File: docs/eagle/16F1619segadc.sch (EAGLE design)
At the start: 21 parts, among them IC1 74HC595N, IC2 PIC16F1619, T1 2N2222, T2 2N2222, T3 2N2222, T4 2N2222

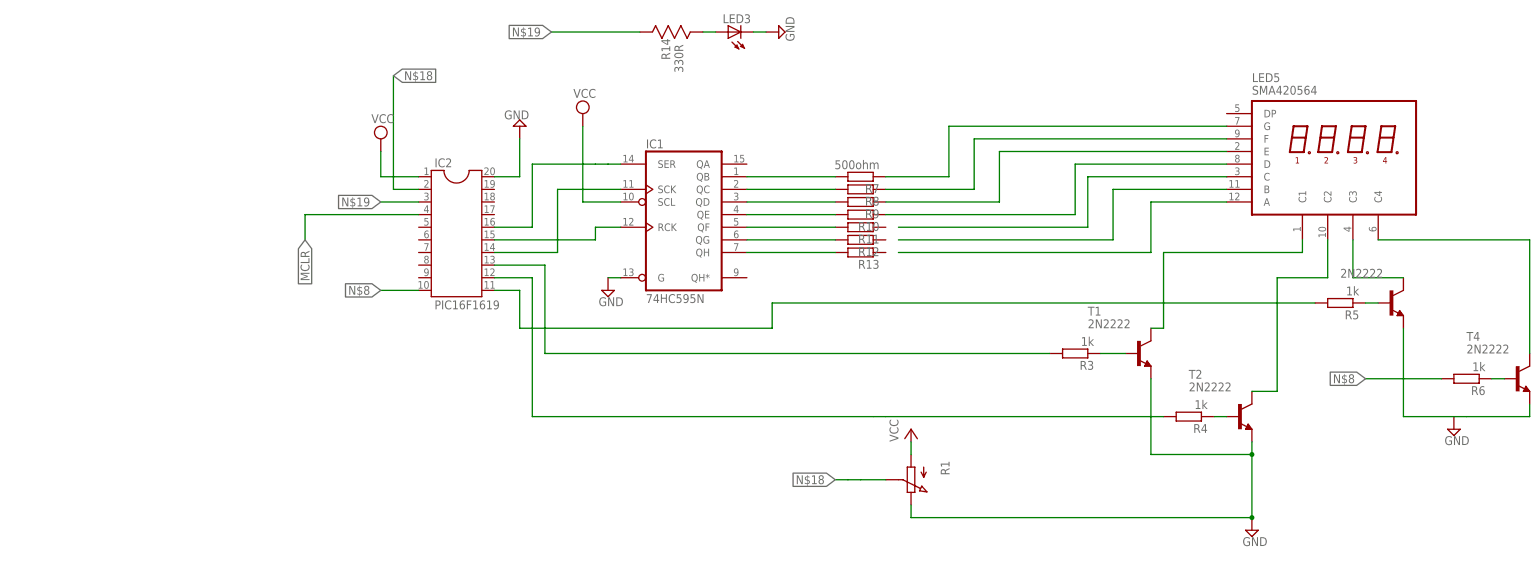
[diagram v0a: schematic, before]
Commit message: change eagle footprint for pic16f1619
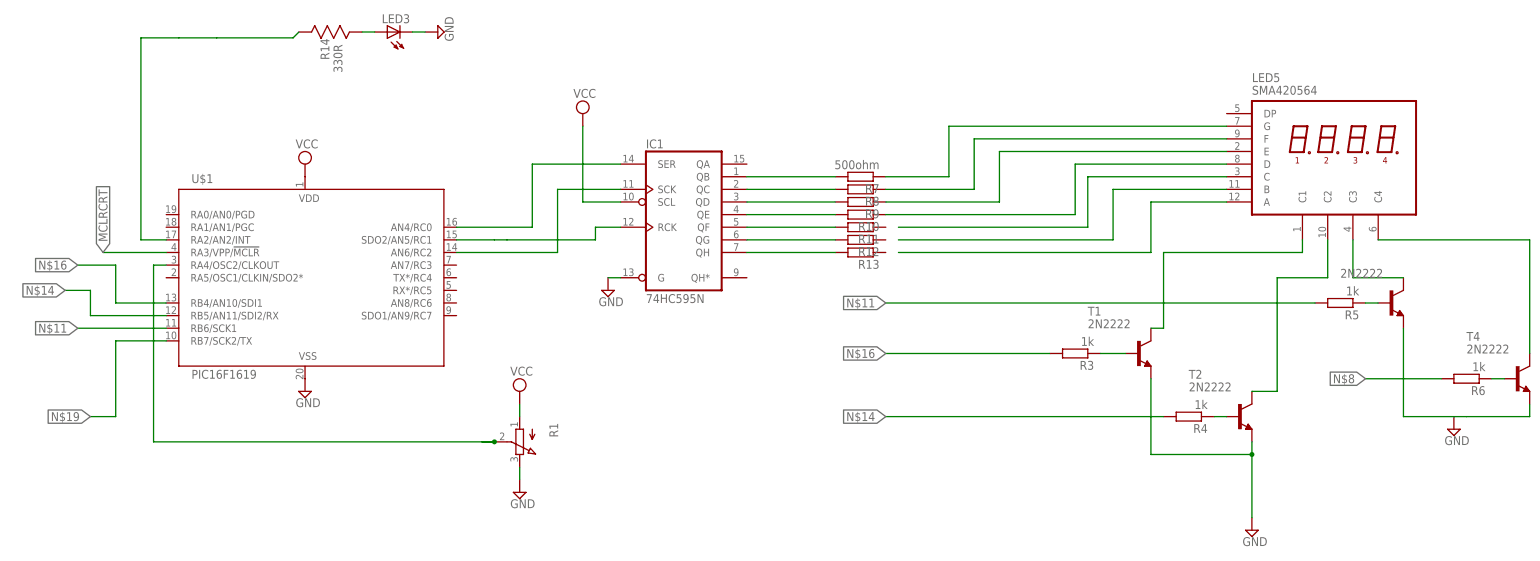
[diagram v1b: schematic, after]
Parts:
- removed IC2: PIC16F1619, ic-package:DIL20
- added U$1: PIC16F1619, SparkFun-IC-Microcontroller:PIC16F1829
- R1: device pot-vitrohm:PC25 -> pot:3RP/1610N
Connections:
- removed net MCLR: IC2.4
- new net MCLRCRT: U$1.RA3/VPP/!MCLR
- net GND: now also U$1.VSS; no longer IC2.20
- net N$1: now also R1.S, U$1.RA4/OSC2/CLKOUT; no longer IC2.10
- net N$11: now also U$1.RB6/SCK1; no longer IC2.11
- net N$14: now also U$1.RB5/AN11/SDI2/RX; no longer IC2.12
- net N$16: now also U$1.RB4/AN10/SDI1; no longer IC2.13
- net N$18: now also R14.R1, U$1.RA2/AN2/INT; no longer IC2.2, R1.S
- net N$19: now also U$1.RB7/SCK2/TX; no longer IC2.3, R14.R1
- net N$3: now also U$1.AN6/RC2; no longer IC2.14
- net N$4: now also U$1.SDO2/AN5/RC1; no longer IC2.15
- net N$7: now also U$1.AN4/RC0; no longer IC2.16
- net VCC: now also U$1.VDD; no longer IC2.1
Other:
- moved on the sheet: LED3, R14

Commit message: adding  new  eagle library footprint to schematic for SMA420564
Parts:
- removed LED5: SMA420564, hp-displays:5082-7414
- added SMA420564: NFD-5641AS, display-nfd:NFD-5641AS
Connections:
- removed net N$8: R6.2
- net N$10: now also SMA420564.P$5; no longer LED5.G
- net N$19: now also R6.2
- net N$2: now also SMA420564.P$9; no longer LED5.C2
- net N$24: now also SMA420564.P$8; no longer LED5.C3
- net N$25: now also SMA420564.P$6; no longer LED5.C4
- net N$26: now also SMA420564.P$11; no longer LED5.A
- net N$27: now also SMA420564.P$7; no longer LED5.B
- net N$28: now also SMA420564.P$1; no longer LED5.E
- net N$29: now also SMA420564.P$4; no longer LED5.C
- net N$30: now also SMA420564.P$2; no longer LED5.D
- net N$5: now also SMA420564.P$12; no longer LED5.C1
- net N$9: now also SMA420564.P$10; no longer LED5.F
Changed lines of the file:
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@@
 <?xml version="1.0" encoding="utf-8"?>
 <!DOCTYPE eagle SYSTEM "eagle.dtd">
-<eagle version="9.3.0">
+<eagle version="9.3.1">
 <drawing>
 <settings>
@@
 <part name="R12" library="eagle-ltspice" library_urn="urn:adsk.eagle:library:217" deviceset="R" device="0204/7" package3d_urn="urn:adsk.eagle:package:13274/1"/>
 <part name="R13" library="eagle-ltspice" library_urn="urn:adsk.eagle:library:217" deviceset="R" device="0204/7" package3d_urn="urn:adsk.eagle:package:13274/1"/>
-<part name="LED5" library="hp-displays" deviceset="5082-7414" device="" value="SMA420564"/>
 <part name="IC1" library="74xx-eu" library_urn="urn:adsk.eagle:library:85" deviceset="74*595" device="N" package3d_urn="urn:adsk.eagle:package:922/2" technology="HC"/>
 <part name="SUPPLY2" library="supply2" library_urn="urn:adsk.eagle:library:372" deviceset="GND" device=""/>
@@
 <part name="SUPPLY7" library="supply2" library_urn="urn:adsk.eagle:library:372" deviceset="GND" device=""/>
 <part name="SUPPLY8" library="supply2" library_urn="urn:adsk.eagle:library:372" deviceset="VCC" device=""/>
+<part name="SMA420564" library="display-nfd" deviceset="NFD-5641AS" device=""/>
 </parts>
 <sheets>
@@
 <attribute name="VALUE" x="85.09" y="64.262" size="1.778" layer="96" rot="R180"/>
 </instance>
-<instance part="LED5" gate="$1" x="160.02" y="91.44" smashed="yes">
-<attribute name="NAME" x="160.02" y="95.25" size="1.778" layer="95"/>
-<attribute name="VALUE" x="160.02" y="92.71" size="1.778" layer="96"/>
-</instance>
 <instance part="IC1" gate="A" x="45.72" y="68.58" smashed="yes">
 <attribute name="NAME" x="38.1" y="81.915" size="1.778" layer="95"/>
@@
 <instance part="SUPPLY8" gate="G$1" x="12.7" y="33.02" smashed="yes">
 <attribute name="VALUE" x="10.795" y="36.195" size="1.778" layer="96"/>
+</instance>
+<instance part="SMA420564" gate="G$1" x="165.1" y="78.74" smashed="yes" rot="MR270">
+<attribute name="NAME" x="170.18" y="94.107" size="1.778" layer="95" rot="MR0"/>
 </instance>
 </instances>
@@
 <wire x1="165.1" y1="33.02" x2="160.02" y2="33.02" width="0.1524" layer="91"/>
 <wire x1="165.1" y1="55.88" x2="165.1" y2="33.02" width="0.1524" layer="91"/>
-<pinref part="LED5" gate="$1" pin="C2"/>
-<wire x1="175.26" y1="63.5" x2="175.26" y2="55.88" width="0.1524" layer="91"/>
-<wire x1="175.26" y1="55.88" x2="165.1" y2="55.88" width="0.1524" layer="91"/>
+<wire x1="165.1" y1="55.88" x2="175.26" y2="55.88" width="0.1524" layer="91"/>
+<wire x1="175.26" y1="55.88" x2="175.26" y2="63.5" width="0.1524" layer="91"/>
+<wire x1="175.26" y1="63.5" x2="195.58" y2="63.5" width="0.1524" layer="91"/>
+<wire x1="195.58" y1="63.5" x2="195.58" y2="76.2" width="0.1524" layer="91"/>
+<pinref part="SMA420564" gate="G$1" pin="P$9"/>
+<wire x1="195.58" y1="76.2" x2="175.26" y2="76.2" width="0.1524" layer="91"/>
 </segment>
 </net>
@@
 <pinref part="R9" gate="G$1" pin="1"/>
 <wire x1="86.36" y1="71.12" x2="109.22" y2="71.12" width="0.1524" layer="91"/>
-<pinref part="LED5" gate="$1" pin="E"/>
 <wire x1="154.94" y1="81.28" x2="109.22" y2="81.28" width="0.1524" layer="91"/>
 <wire x1="109.22" y1="81.28" x2="109.22" y2="71.12" width="0.1524" layer="91"/>
+<pinref part="SMA420564" gate="G$1" pin="P$1"/>
 </segment>
 </net>
@@
 <wire x1="86.36" y1="73.66" x2="104.14" y2="73.66" width="0.1524" layer="91"/>
 <wire x1="104.14" y1="73.66" x2="104.14" y2="83.82" width="0.1524" layer="91"/>
-<pinref part="LED5" gate="$1" pin="F"/>
 <wire x1="104.14" y1="83.82" x2="154.94" y2="83.82" width="0.1524" layer="91"/>
+<pinref part="SMA420564" gate="G$1" pin="P$10"/>
 </segment>
 </net>
@@
 <pinref part="R7" gate="G$1" pin="1"/>
 <wire x1="86.36" y1="76.2" x2="99.06" y2="76.2" width="0.1524" layer="91"/>
-<pinref part="LED5" gate="$1" pin="G"/>
 <wire x1="154.94" y1="86.36" x2="99.06" y2="86.36" width="0.1524" layer="91"/>
 <wire x1="99.06" y1="86.36" x2="99.06" y2="76.2" width="0.1524" layer="91"/>
+<pinref part="SMA420564" gate="G$1" pin="P$5"/>
 </segment>
 </net>
@@
 <wire x1="139.7" y1="45.72" x2="142.24" y2="45.72" width="0.1524" layer="91"/>
 <wire x1="142.24" y1="45.72" x2="142.24" y2="60.96" width="0.1524" layer="91"/>
-<wire x1="142.24" y1="60.96" x2="170.18" y2="60.96" width="0.1524" layer="91"/>
-<pinref part="LED5" gate="$1" pin="C1"/>
-<wire x1="170.18" y1="60.96" x2="170.18" y2="63.5" width="0.1524" layer="91"/>
-</segment>
-</net>
-<net name="N$24" class="0">
-<segment>
-<pinref part="LED5" gate="$1" pin="C3"/>
-<wire x1="180.34" y1="63.5" x2="180.34" y2="55.88" width="0.1524" layer="91"/>
-<pinref part="T3" gate="G$1" pin="C"/>
-<wire x1="180.34" y1="55.88" x2="190.5" y2="55.88" width="0.1524" layer="91"/>
+<wire x1="142.24" y1="60.96" x2="200.66" y2="60.96" width="0.1524" layer="91"/>
+<wire x1="200.66" y1="60.96" x2="200.66" y2="78.74" width="0.1524" layer="91"/>
+<pinref part="SMA420564" gate="G$1" pin="P$12"/>
+<wire x1="200.66" y1="78.74" x2="175.26" y2="78.74" width="0.1524" layer="91"/>
 </segment>
 </net>
 <net name="N$25" class="0">
 <segment>
-<pinref part="LED5" gate="$1" pin="C4"/>
 <pinref part="T4" gate="G$1" pin="C"/>
-<wire x1="185.42" y1="63.5" x2="215.9" y2="63.5" width="0.1524" layer="91"/>
-<wire x1="215.9" y1="63.5" x2="215.9" y2="40.64" width="0.1524" layer="91"/>
+<wire x1="215.9" y1="71.12" x2="215.9" y2="40.64" width="0.1524" layer="91"/>
+<pinref part="SMA420564" gate="G$1" pin="P$6"/>
+<wire x1="215.9" y1="71.12" x2="175.26" y2="71.12" width="0.1524" layer="91"/>
 </segment>
 </net>
@@
 <wire x1="88.9" y1="60.96" x2="139.7" y2="60.96" width="0.1524" layer="91"/>
 <wire x1="139.7" y1="60.96" x2="139.7" y2="71.12" width="0.1524" layer="91"/>
-<pinref part="LED5" gate="$1" pin="A"/>
 <wire x1="139.7" y1="71.12" x2="154.94" y2="71.12" width="0.1524" layer="91"/>
+<pinref part="SMA420564" gate="G$1" pin="P$11"/>
 </segment>
 </net>
@@
 <wire x1="88.9" y1="63.5" x2="132.08" y2="63.5" width="0.1524" layer="91"/>
 <wire x1="132.08" y1="63.5" x2="132.08" y2="73.66" width="0.1524" layer="91"/>
-<pinref part="LED5" gate="$1" pin="B"/>
 <wire x1="132.08" y1="73.66" x2="154.94" y2="73.66" width="0.1524" layer="91"/>
+<pinref part="SMA420564" gate="G$1" pin="P$7"/>
 </segment>
 </net>
@@
 <wire x1="88.9" y1="66.04" x2="127" y2="66.04" width="0.1524" layer="91"/>
 <wire x1="127" y1="66.04" x2="127" y2="76.2" width="0.1524" layer="91"/>
-<pinref part="LED5" gate="$1" pin="C"/>
 <wire x1="127" y1="76.2" x2="154.94" y2="76.2" width="0.1524" layer="91"/>
+<pinref part="SMA420564" gate="G$1" pin="P$4"/>
 </segment>
 </net>
@@
 <wire x1="86.36" y1="68.58" x2="124.46" y2="68.58" width="0.1524" layer="91"/>
 <wire x1="124.46" y1="68.58" x2="124.46" y2="78.74" width="0.1524" layer="91"/>
-<pinref part="LED5" gate="$1" pin="D"/>
 <wire x1="124.46" y1="78.74" x2="154.94" y2="78.74" width="0.1524" layer="91"/>
+<pinref part="SMA420564" gate="G$1" pin="P$2"/>
 </segment>
 </net>
@@
 <pinref part="U$1" gate="1" pin="AN4/RC0"/>
 <wire x1="15.24" y1="66.04" x2="0" y2="66.04" width="0.1524" layer="91"/>
-</segment>
-</net>
-<net name="N$8" class="0">
-<segment>
-<pinref part="R6" gate="G$1" pin="2"/>
-<wire x1="198.12" y1="35.56" x2="182.88" y2="35.56" width="0.1524" layer="91"/>
-<label x="182.88" y="35.56" size="1.778" layer="95" rot="R180" xref="yes"/>
 </segment>
 </net>
@@
 <wire x1="-68.58" y1="27.94" x2="-73.66" y2="27.94" width="0.1524" layer="91"/>
 </segment>
-</net>
+<segment>
+<pinref part="R6" gate="G$1" pin="2"/>
+<wire x1="198.12" y1="35.56" x2="182.88" y2="35.56" width="0.1524" layer="91"/>
+<label x="182.88" y="35.56" size="1.778" layer="95" rot="R180" xref="yes"/>
+</segment>
+</net>
+<net name="N$24" class="0">
+<segment>
+<pinref part="T3" gate="G$1" pin="C"/>
+<wire x1="190.5" y1="55.88" x2="190.5" y2="73.66" width="0.1524" layer="91"/>
+<pinref part="SMA420564" gate="G$1" pin="P$8"/>
+<wire x1="190.5" y1="73.66" x2="175.26" y2="73.66" width="0.1524" layer="91"/>
+</segment>
+</net>
